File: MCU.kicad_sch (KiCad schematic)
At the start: 2 parts, among them U2 ATmega2560-16A, Y1 CSTCE16M0V53-R0

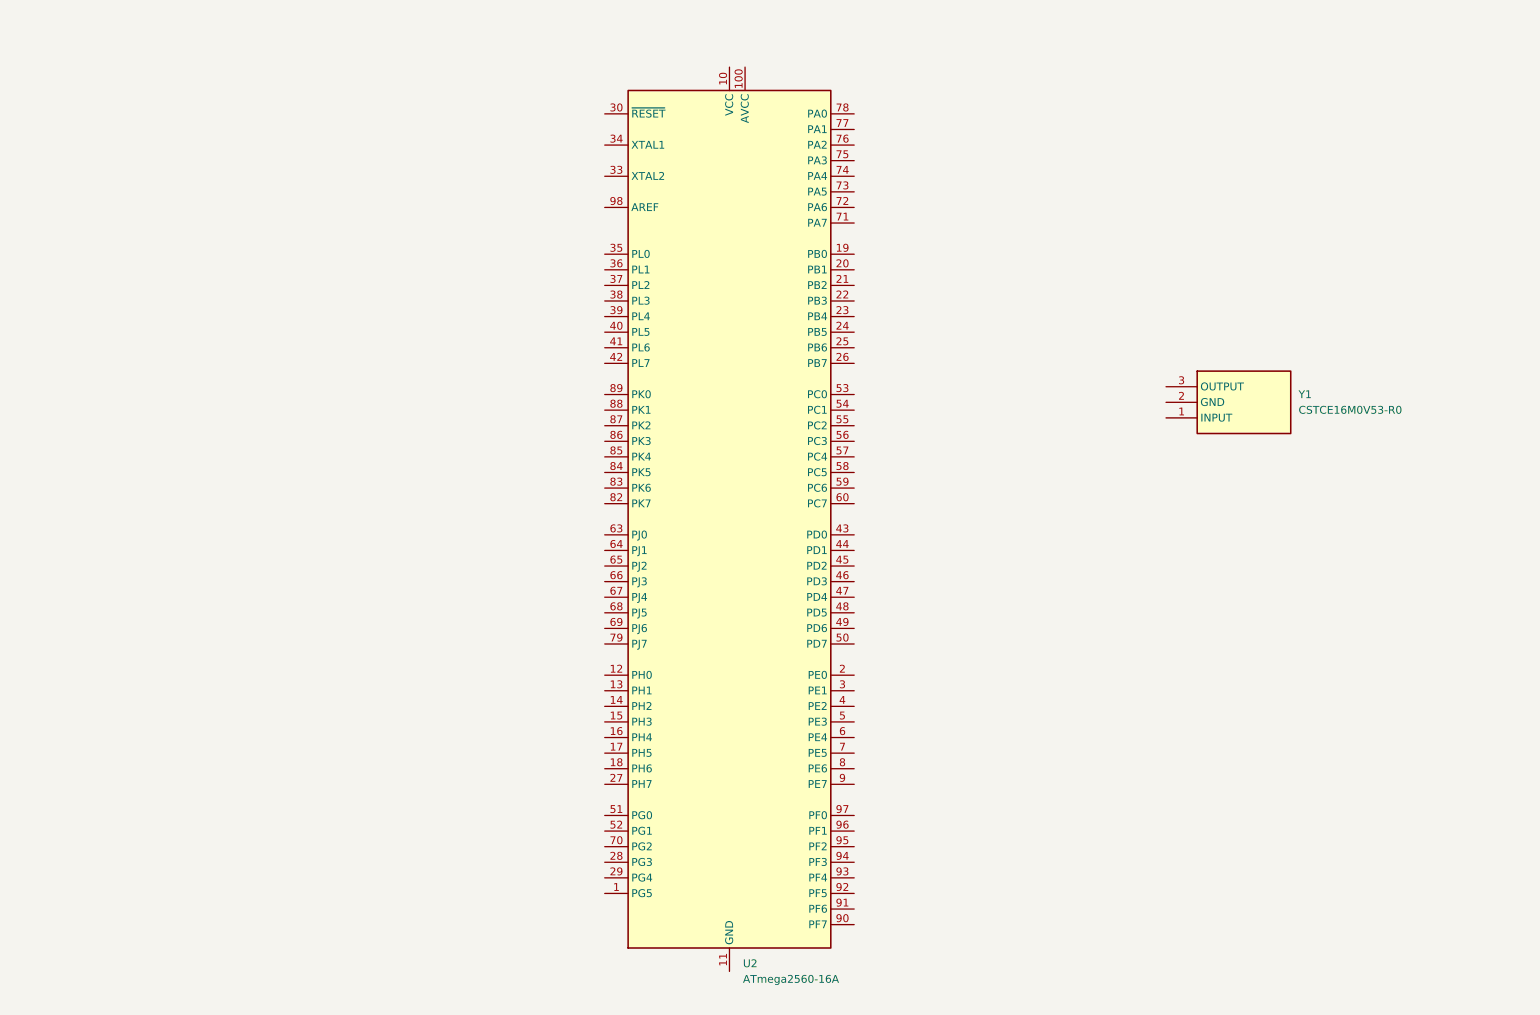
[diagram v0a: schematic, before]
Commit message: updated MCU VCC
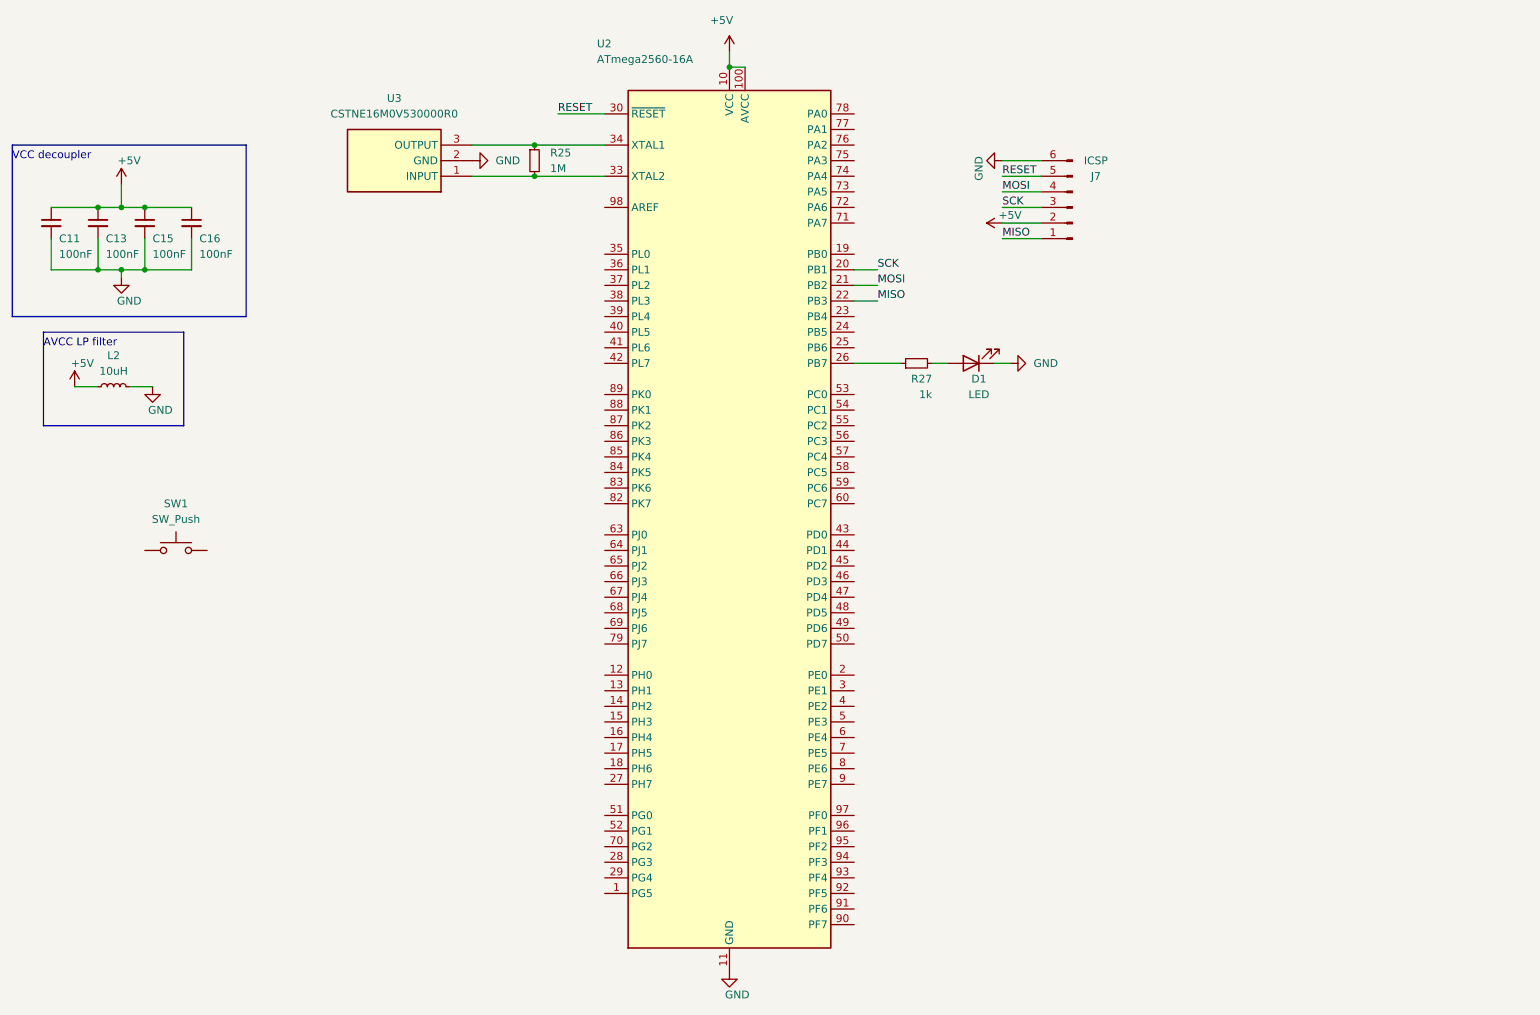
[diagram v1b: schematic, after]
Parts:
- removed Y1: CSTCE16M0V53-R0, SamacSys_Parts:CSTCE16M0V53R0, symbol SamacSys_Parts:CSTCE16M0V53-R0
- added C11, C13, C15, C16: 100nF, symbol Device:C_Small
- added D1: LED, symbol Device:LED
- added J7: ICSP, symbol Connector:Conn_01x06_Pin
- added L2: 10uH, symbol Device:L_Small
- added R25: 1M, symbol Device:R_Small
- added R27: 1k, symbol Device:R_Small
- added SW1: SW_Push, symbol Switch:SW_Push
- added U3: CSTNE16M0V530000R0, SamacSys_Parts:CSTNE16M0V530000R0, symbol SamacSys_Parts:CSTNE16M0V530000R0
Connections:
- net +5V: now reaches U2.10 (VCC), U2.31 (VCC), U2.61 (VCC), U2.80 (VCC)
- net +5V: now also U2.100 (AVCC), C11.1, C13.1, C15.1, C16.1, J7.2 (Pin_2), L2.1
- net GND: now reaches U2.11 (GND), U2.32 (GND), U2.62 (GND), U2.81 (GND), U2.99 (GND)
- net GND: now also C11.2, C13.2, C15.2, C16.2, D1.1 (K), J7.6 (Pin_6), L2.2, U3.2 (GND)
- net SCK: now reaches U2.20 (PB1)
- net SCK: now also J7.3 (Pin_3)
- net MOSI: now reaches U2.21 (PB2)
- net MOSI: now also J7.4 (Pin_4)
- net MISO: now reaches U2.22 (PB3)
- net MISO: now also J7.1 (Pin_1)
- net at U2.26 (PB7): now also R27.1
- net RESET: now reaches U2.30 (~{RESET})
- net RESET: now also J7.5 (Pin_5)
- net at U2.33 (XTAL2): now also R25.2, U3.1 (INPUT)
- net at U2.34 (XTAL1): now also R25.1, U3.3 (OUTPUT)
- new net: D1.2 (A), R27.2
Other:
- note added: "AVCC LP filter"
- note added: "VCC decoupler"

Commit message: MCU migration completed
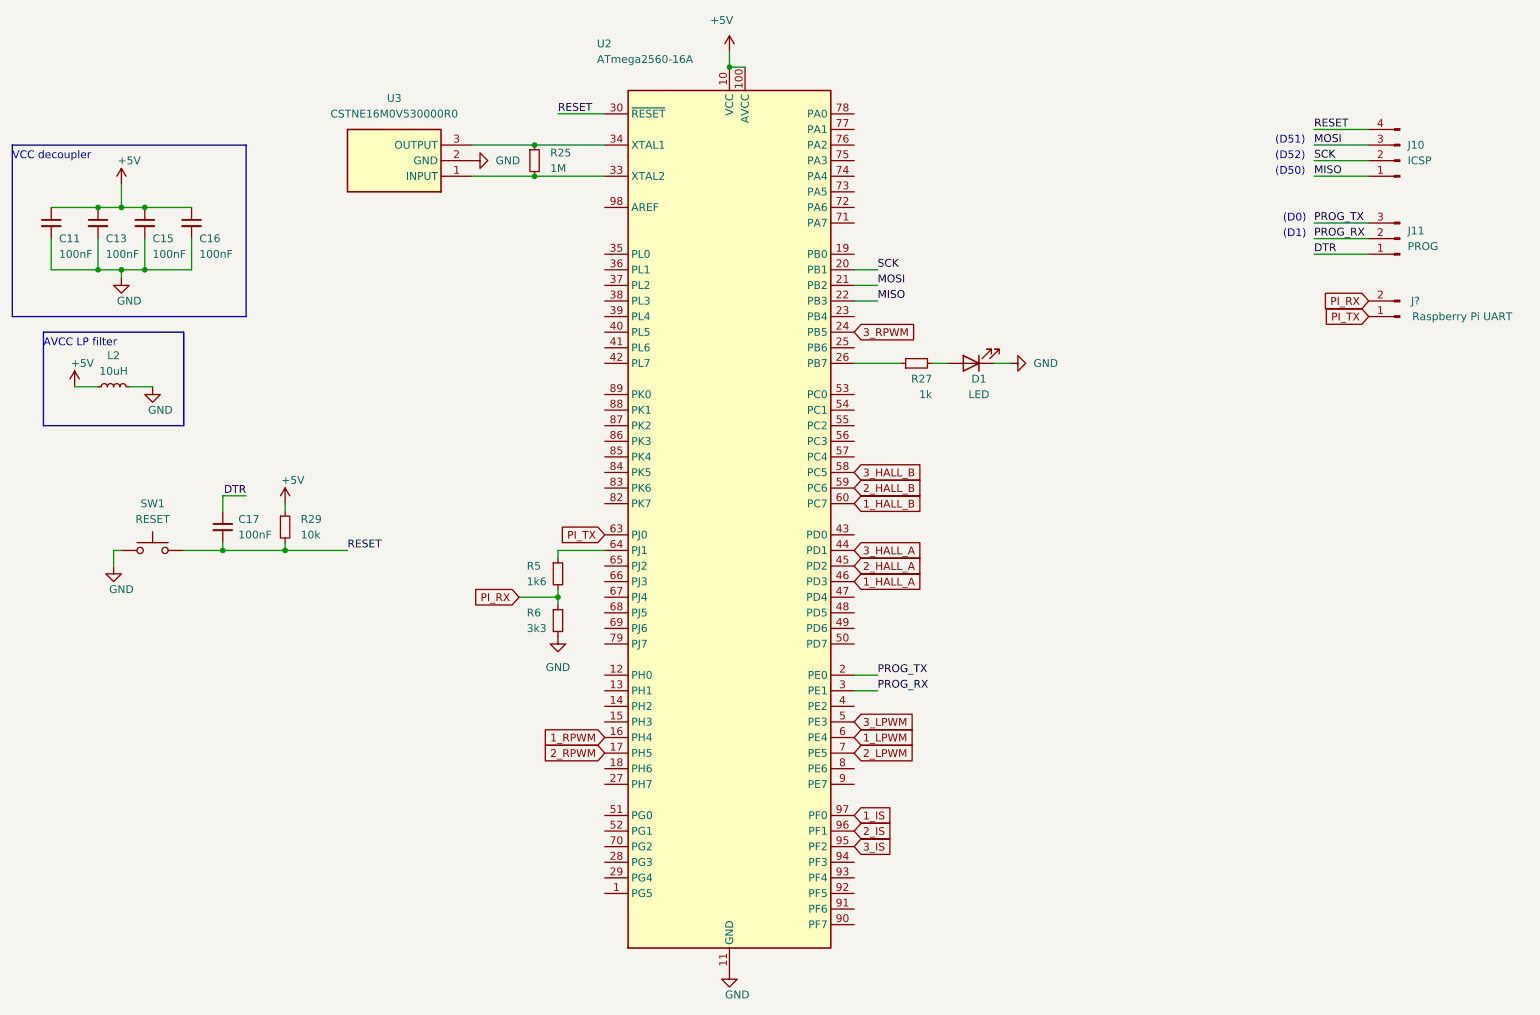
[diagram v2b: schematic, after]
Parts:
- removed J7: ICSP, symbol Connector:Conn_01x06_Pin
- added C17: 100nF, symbol Device:C_Small
- added J10: ICSP, symbol Connector:Conn_01x04_Pin
- added J11: PROG, symbol Connector:Conn_01x03_Pin
- added J?: Raspberry Pi UART, Connector_PinHeader_2.54mm:PinHeader_1x02_P2.54mm_Vertical, symbol Connector:Conn_01x02_Pin
- added R29: 10k, symbol Device:R_Small
- added R5: 1k6, Resistor_SMD:R_0805_2012Metric_Pad1.20x1.40mm_HandSolder, symbol Device:R_Small
- added R6: 3k3, Resistor_SMD:R_1206_3216Metric_Pad1.30x1.75mm_HandSolder, symbol Device:R_Small
- SW1: value SW_Push -> RESET
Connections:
- net +5V: now also R29.1
- net GND: now also SW1.1, R6.2
- net MISO: now also J10.1 (Pin_1)
- net MOSI: now also J10.3 (Pin_3)
- net RESET: now also SW1.2, C17.2, J10.4 (Pin_4), R29.2
- net SCK: now also J10.2 (Pin_2)
- net 1_RPWM: now reaches U2.16 (PH4)
- net 2_RPWM: now reaches U2.17 (PH5)
- net PROG_TX: now reaches U2.2 (PE0)
- net PROG_TX: now also J11.3 (Pin_3)
- net 3_RPWM: now reaches U2.24 (PB5)
- net PROG_RX: now reaches U2.3 (PE1)
- net PROG_RX: now also J11.2 (Pin_2)
- net 3_HALL_A: now reaches U2.44 (PD1)
- net 2_HALL_A: now reaches U2.45 (PD2)
- net 1_HALL_A: now reaches U2.46 (PD3)
- net 3_LPWM: now reaches U2.5 (PE3)
- net 3_HALL_B: now reaches U2.58 (PC5)
- net 2_HALL_B: now reaches U2.59 (PC6)
- net 1_LPWM: now reaches U2.6 (PE4)
- net 1_HALL_B: now reaches U2.60 (PC7)
- net PI_TX: now reaches U2.63 (PJ0)
- net PI_TX: now also J?.1 (Pin_1)
- net at U2.64 (PJ1): now also R5.1
- net 2_LPWM: now reaches U2.7 (PE5)
- net 3_IS: now reaches U2.95 (PF2)
- net 2_IS: now reaches U2.96 (PF1)
- net 1_IS: now reaches U2.97 (PF0)
- new net DTR: C17.1, J11.1 (Pin_1)
- new net PI_RX: J?.2 (Pin_2), R5.2, R6.1
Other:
- note added: "(D0)"
- note added: "(D1)"
- note added: "(D50)"
- note added: "(D51)"
- note added: "(D52)"
- title: (none) -> RBC by UGS
- moved on the sheet: SW1

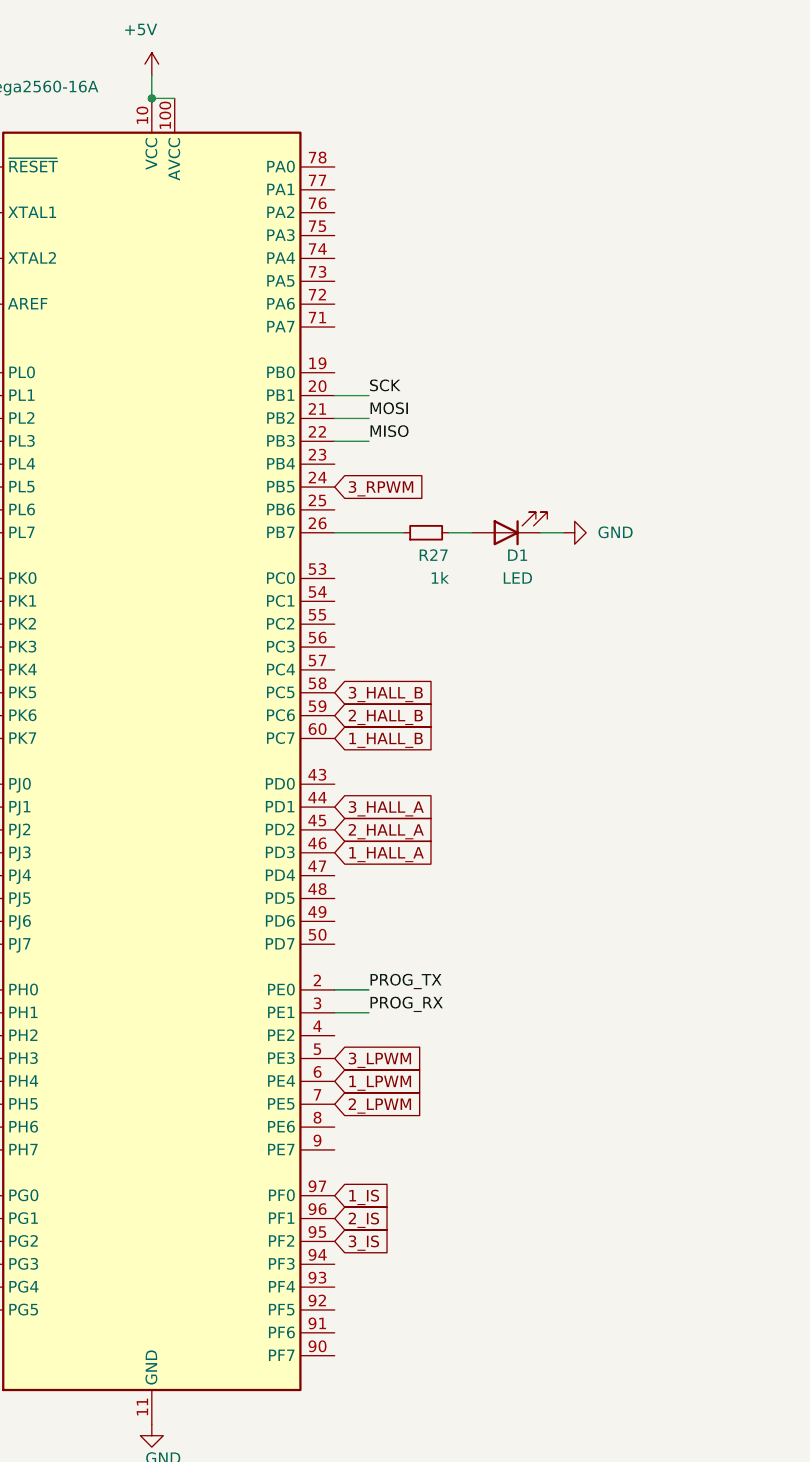
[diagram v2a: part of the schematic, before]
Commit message: implemented battery level detection
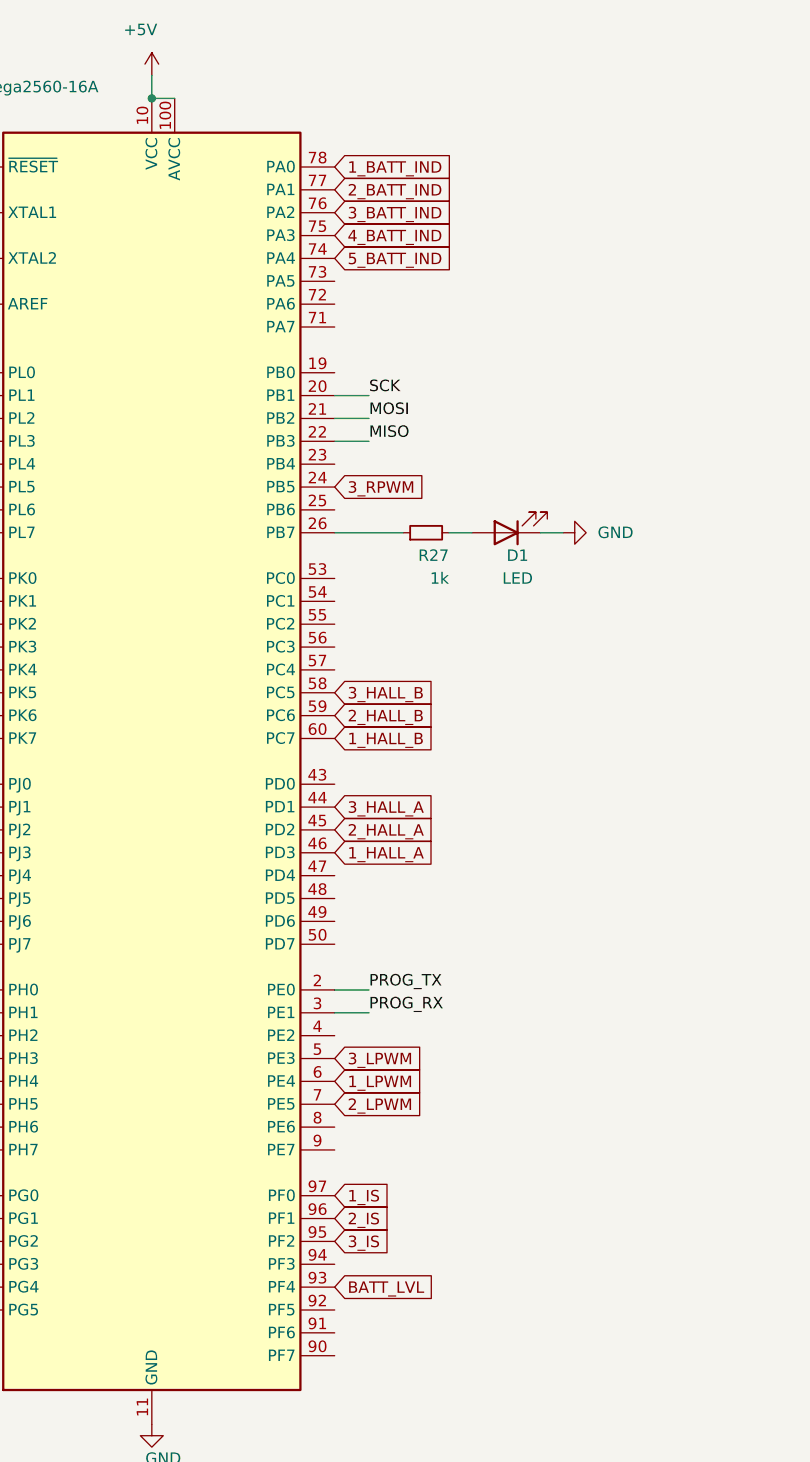
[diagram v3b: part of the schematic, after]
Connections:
- net 5_BATT_IND: now reaches U2.74 (PA4)
- net 4_BATT_IND: now reaches U2.75 (PA3)
- net 3_BATT_IND: now reaches U2.76 (PA2)
- net 2_BATT_IND: now reaches U2.77 (PA1)
- net 1_BATT_IND: now reaches U2.78 (PA0)
- net BATT_LVL: now reaches U2.93 (PF4)
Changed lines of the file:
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@@
+    )
+  )
+  (global_label "3_BATT_IND" (shape input) (at 151.13 36.83 0) (fields_autoplaced)
+    (effects (font (size 1.27 1.27)) (justify left))
+    (property "Intersheetrefs" "${INTERSHEET_REFS}" (at 164.759 36.83 0)
+      (effects (font (size 1.27 1.27)) (justify left) hide)
     )
   )
@@
     )
   )
+  (global_label "4_BATT_IND" (shape input) (at 151.13 39.37 0) (fields_autoplaced)
+    (effects (font (size 1.27 1.27)) (justify left))
+    (property "Intersheetrefs" "${INTERSHEET_REFS}" (at 164.759 39.37 0)
+      (effects (font (size 1.27 1.27)) (justify left) hide)
+    )
+  )
   (global_label "1_LPWM" (shape input) (at 151.13 133.35 0) (fields_autoplaced)
     (effects (font (size 1.27 1.27)) (justify left))
@@
     )
   )
+  (global_label "5_BATT_IND" (shape input) (at 151.13 41.91 0) (fields_autoplaced)
+    (effects (font (size 1.27 1.27)) (justify left))
+    (property "Intersheetrefs" "${INTERSHEET_REFS}" (at 164.759 41.91 0)
+      (effects (font (size 1.27 1.27)) (justify left) hide)
+    )
+  )
   (global_label "3_IS" (shape input) (at 151.13 151.13 0) (fields_autoplaced)
     (effects (font (size 1.27 1.27)) (justify left))
     (property "Intersheetrefs" "${INTERSHEET_REFS}" (at 158.1066 151.13 0)
+      (effects (font (size 1.27 1.27)) (justify left) hide)
+    )
+  )
+  (global_label "1_BATT_IND" (shape input) (at 151.13 31.75 0) (fields_autoplaced)
+    (effects (font (size 1.27 1.27)) (justify left))
+    (property "Intersheetrefs" "${INTERSHEET_REFS}" (at 164.759 31.75 0)
+      (effects (font (size 1.27 1.27)) (justify left) hide)
+    )
+  )
+  (global_label "2_BATT_IND" (shape input) (at 151.13 34.29 0) (fields_autoplaced)
+    (effects (font (size 1.27 1.27)) (justify left))
+    (property "Intersheetrefs" "${INTERSHEET_REFS}" (at 164.759 34.29 0)
       (effects (font (size 1.27 1.27)) (justify left) hide)
     )
@@
     )
   )
+  (global_label "BATT_LVL" (shape input) (at 151.13 156.21 0) (fields_autoplaced)
+    (effects (font (size 1.27 1.27)) (justify left))
+    (property "Intersheetrefs" "${INTERSHEET_REFS}" (at 162.5214 156.21 0)
+      (effects (font (size 1.27 1.27)) (justify left) hide)
+    )
+  )

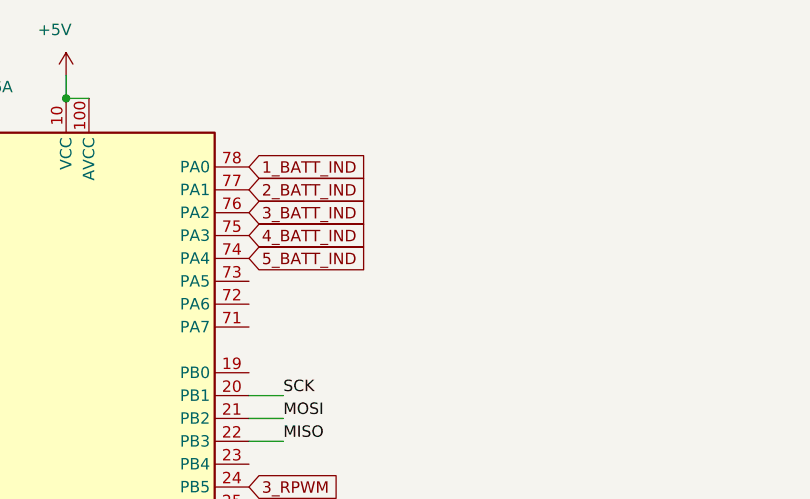
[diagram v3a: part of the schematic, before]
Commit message: completed 12V regulators
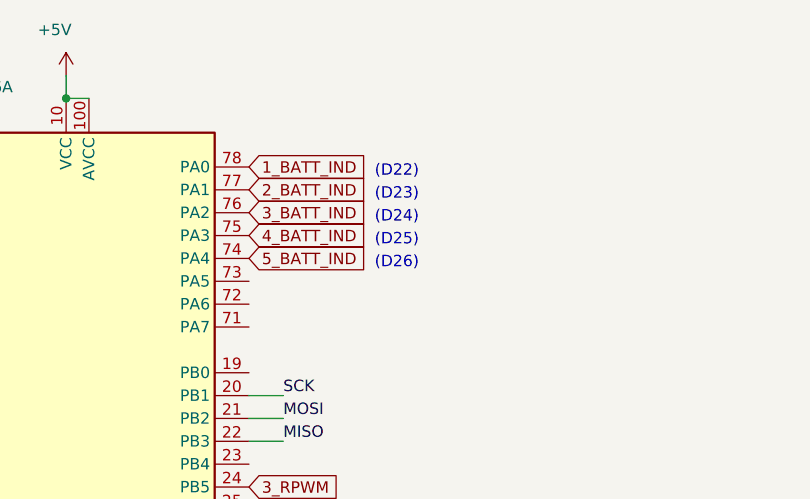
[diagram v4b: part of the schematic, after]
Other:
- note added: "(D22)"
- note added: "(D23)"
- note added: "(D24)"
- note added: "(D25)"
- note added: "(D26)"
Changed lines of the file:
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@@
+    (effects (font (size 1.27 1.27)) (justify left bottom))
+  )
+  (text "(D22)" (at 165.1 33.02 0)
+    (effects (font (size 1.27 1.27)) (justify left bottom))
+  )
+  (text "(D23)" (at 165.1 35.56 0)
+    (effects (font (size 1.27 1.27)) (justify left bottom))
+  )
+  (text "(D25)" (at 165.1 40.64 0)
+    (effects (font (size 1.27 1.27)) (justify left bottom))
+  )
+  (text "(D26)" (at 165.1 43.18 0)
     (effects (font (size 1.27 1.27)) (justify left bottom))
   )
@@
     (effects (font (size 1.27 1.27)) (justify left bottom))
   )
+  (text "(D24)" (at 165.1 38.1 0)
+    (effects (font (size 1.27 1.27)) (justify left bottom))
+  )
